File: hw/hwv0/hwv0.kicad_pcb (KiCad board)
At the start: 2 copper layers, 29 parts, among them J1 AVR-ISP-6, J2 PWR_IN_7-12V, J3 RS232, SW1 SW_Push, U1 ATtiny84A-MU, U2 LCD_1602, U3 MAX232I, U4 L7805

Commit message: Almost completed PCB
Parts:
- moved C5 91.4 mm to (103.1, 151.3), turned to 0 degrees
- moved SW1 91.2 mm to (83.6, 150.8), turned to 90 degrees
- moved TP7 89.5 mm to (108.7, 154.2)
- moved TP6 85.0 mm to (111.4, 154.3)
- moved J3 80.1 mm to (121.7, 139.3)
- moved U3 77.7 mm to (109.2, 146.1)
- moved C6 77.3 mm to (103.2, 149.7)
- moved C4 77.2 mm to (103.9, 146.1)
- moved C3 77.1 mm to (103.9, 142.9)
- moved C8 76.4 mm to (75.8, 154.5), turned to 0 degrees
- moved StrainGauge1 73.1 mm to (97.2, 158.4), turned to 180 degrees
- moved R1 70.2 mm to (92.1, 145.0), turned to 0 degrees
- moved D1 68.8 mm to (92.1, 142.9), turned to 180 degrees
- moved J1 67.7 mm to (94.8, 137.6), turned to 270 degrees
- moved TP2 66.6 mm to (83.2, 157.3), turned to 0 degrees
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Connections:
- J1 pad 1: (no net) -> /MISO
- J1 pad 3: (no net) -> /SCK
- J1 pad 4: (no net) -> /MOSI
- StrainGauge1 pad 3: /STRAINGAUGE- -> /SCK
- TP4 pad 1: /STRAINGAUGE- -> /SCK
- U1 pad 1: /STRAINGAUGE- -> /SCK
- U1 pad 16: Net-(U1-Pad16) -> /MOSI
- U1 pad 20: Net-(U1-Pad20) -> /MISO
- U2 pad 13: Net-(U1-Pad16) -> /MOSI
- U2 pad 14: Net-(U1-Pad20) -> /MISO
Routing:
- net +5V: track 0.00 -> 196.1 mm
- net GNDD: track 0.00 -> 146.3 mm
- net /MISO: track 0.00 -> 91.7 mm
- net /MOSI: track 0.00 -> 87.7 mm, vias 0 -> 1
- net Net-(U1-Pad15): track 0.00 -> 68.5 mm
- net /RX_L: track 0.00 -> 58.1 mm
- net /SCK: track 0.00 -> 49.8 mm
- net /~RST: track 0.00 -> 49.8 mm, vias 0 -> 1
- net /TX_L: track 0.00 -> 44.6 mm
- net /STRAINGAUGE+: track 0.00 -> 41.9 mm
- net /P_sen_analogIN: track 0.00 -> 23.9 mm
- net Net-(U1-Pad11): track 0.00 -> 19.1 mm
- net Net-(U1-Pad14): track 0.00 -> 18.0 mm
- net /RX_H: track 0.00 -> 16.6 mm
- net Net-(C5-Pad2): track 0.00 -> 15.5 mm
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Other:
- board outline added: 60.3 x 54.6 mm
- net class Default: trace_width 0.25 -> 0.3

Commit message: finished PCB
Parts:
- moved C8 2.02 mm to (77.8, 154.6)
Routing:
- net +5V: track 196.1 -> 250.8 mm
- net Net-(C7-Pad1): track 0.00 -> 20.8 mm
- added copper zone on B.Cu, net GNDD
- added copper zone on F.Cu, net GNDD
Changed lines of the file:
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@@
     (thickness 1.6)
     (drawings 6)
-    (tracks 260)
+    (tracks 281)
     (zones 0)
     (modules 29)
@@
   )
   (module Capacitor_SMD:CP_Elec_6.3x3 (layer F.Cu)
-    (at 75.7555 154.4955)
+    (at 77.7748 154.6352)
     (descr "SMT capacitor, aluminium electrolytic, 6.3x3, Nichicon ")
     (tags "Capacitor Electrolytic")
@@
   (segment (start 95.631 118.999) (end 95.631 120.269) (width 0.3) (layer F.Cu) (net 1))
   (segment (start 95.9485 118.6815) (end 95.631 118.999) (width 0.3) (layer F.Cu) (net 1))
+  (segment (start 97.1785 158.4325) (end 97.1785 160.0219) (width 0.5) (layer F.Cu) (net 1))
+  (segment (start 97.1785 160.0219) (end 96.3676 160.8328) (width 0.5) (layer F.Cu) (net 1))
+  (segment (start 96.3676 160.8328) (end 88.2904 160.8328) (width 0.5) (layer F.Cu) (net 1))
+  (segment (start 75.0748 150.9463) (end 73.05 148.9215) (width 1) (layer F.Cu) (net 1))
+  (segment (start 75.0748 154.6352) (end 75.0748 150.9463) (width 1) (layer F.Cu) (net 1))
+  (segment (start 88.2904 160.8328) (end 77.0636 160.8328) (width 0.5) (layer F.Cu) (net 1))
+  (segment (start 75.0748 158.844) (end 75.0748 154.6352) (width 0.5) (layer F.Cu) (net 1))
+  (segment (start 77.0636 160.8328) (end 75.0748 158.844) (width 0.5) (layer F.Cu) (net 1))
+  (segment (start 92.888 147.4976) (end 92.888 145.034) (width 0.5) (layer F.Cu) (net 1))
+  (segment (start 90.5764 149.8092) (end 92.888 147.4976) (width 0.5) (layer F.Cu) (net 1))
+  (segment (start 90.5764 153.3144) (end 90.5764 149.8092) (width 0.5) (layer F.Cu) (net 1))
+  (segment (start 87.3252 156.5656) (end 90.5764 153.3144) (width 0.5) (layer F.Cu) (net 1))
+  (segment (start 88.2904 160.8328) (end 87.3252 160.8328) (width 0.5) (layer F.Cu) (net 1))
+  (segment (start 87.3252 160.8328) (end 87.3252 156.5656) (width 0.5) (layer F.Cu) (net 1))
   (segment (start 76.2 116.300393) (end 76.10405 116.204443) (width 0.25) (layer F.Cu) (net 2))
   (segment (start 76.2 121.92) (end 76.2 116.300393) (width 0.25) (layer F.Cu) (net 2))
@@
   (segment (start 93.649451 150.064249) (end 93.649451 150.818555) (width 0.2) (layer F.Cu) (net 12))
   (segment (start 94.7082 149.0055) (end 93.649451 150.064249) (width 0.2) (layer F.Cu) (net 12))
-  (segment (start 92.1785 153.266605) (end 92.027451 153.115556) (width 0.3) (layer F.Cu) (net 24))
-  (segment (start 92.1785 158.4325) (end 92.1785 153.266605) (width 0.3) (layer F.Cu) (net 24))
-  (segment (start 92.027451 151.990555) (end 93.199451 150.818555) (width 0.2) (layer F.Cu) (net 24))
-  (segment (start 92.027451 153.115556) (end 92.027451 151.990555) (width 0.2) (layer F.Cu) (net 24))
-  (segment (start 98.675433 125.735663) (end 99.075433 125.735663) (width 0.2) (layer F.Cu) (net 24))
-  (segment (start 99.075433 125.735663) (end 99.100433 125.710663) (width 0.2) (layer F.Cu) (net 24))
-  (segment (start 99.100433 125.710663) (end 100.373463 125.710663) (width 0.2) (layer F.Cu) (net 24))
-  (segment (start 100.373463 125.710663) (end 101.9465 127.2837) (width 0.2) (layer F.Cu) (net 24))
-  (segment (start 101.9465 127.2837) (end 101.9465 138.5273) (width 0.2) (layer F.Cu) (net 24))
-  (segment (start 99.4065 141.0673) (end 99.4065 146.8458) (width 0.2) (layer F.Cu) (net 24))
-  (segment (start 99.4065 146.8458) (end 97.6968 148.5555) (width 0.2) (layer F.Cu) (net 24))
-  (segment (start 97.6968 148.5555) (end 94.5218 148.5555) (width 0.2) (layer F.Cu) (net 24))
-  (segment (start 94.5218 148.5555) (end 93.199451 149.877849) (width 0.2) (layer F.Cu) (net 24))
-  (segment (start 93.199451 149.877849) (end 93.199451 150.818555) (width 0.2) (layer F.Cu) (net 24))
   (segment (start 111.898557 146.73705) (end 114.16155 146.73705) (width 0.3) (layer F.Cu) (net 13))
   (segment (start 114.16155 146.73705) (end 115.443 148.0185) (width 0.3) (layer F.Cu) (net 13))
@@
   (segment (start 121.700556 144.855049) (end 116.407049 144.855049) (width 0.4) (layer F.Cu) (net 20))
   (segment (start 116.407049 144.855049) (end 115.74905 144.19705) (width 0.4) (layer F.Cu) (net 20))
+  (segment (start 76.6807 135.8665) (end 73.9775 135.8665) (width 1) (layer F.Cu) (net 21))
+  (segment (start 81.4705 134.3965) (end 78.1507 134.3965) (width 1) (layer F.Cu) (net 21))
+  (segment (start 78.1507 134.3965) (end 76.6807 135.8665) (width 1) (layer F.Cu) (net 21))
+  (segment (start 73.3 144.3215) (end 73.05 144.3215) (width 1) (layer F.Cu) (net 21))
+  (segment (start 76.6064 141.0151) (end 73.3 144.3215) (width 1) (layer F.Cu) (net 21))
+  (segment (start 76.6064 135.8392) (end 76.6064 141.0151) (width 1) (layer F.Cu) (net 21))
+  (segment (start 73.9775 135.8665) (end 76.5791 135.8665) (width 1) (layer F.Cu) (net 21))
+  (segment (start 76.5791 135.8665) (end 76.6064 135.8392) (width 1) (layer F.Cu) (net 21))
   (segment (start 114.20405 119.34895) (end 114.173 119.38) (width 0.4) (layer F.Cu) (net 22))
   (segment (start 114.173 116.235493) (end 114.20405 116.204443) (width 0.3) (layer F.Cu) (net 22))
@@
   (segment (start 94.757951 131.316855) (end 94.251096 130.81) (width 0.25) (layer F.Cu) (net 23))
   (segment (start 94.757951 137.558056) (end 94.757951 131.316855) (width 0.25) (layer F.Cu) (net 23))
+  (segment (start 92.1785 153.266605) (end 92.027451 153.115556) (width 0.3) (layer F.Cu) (net 24))
+  (segment (start 92.1785 158.4325) (end 92.1785 153.266605) (width 0.3) (layer F.Cu) (net 24))
+  (segment (start 92.027451 151.990555) (end 93.199451 150.818555) (width 0.2) (layer F.Cu) (net 24))
+  (segment (start 92.027451 153.115556) (end 92.027451 151.990555) (width 0.2) (layer F.Cu) (net 24))
+  (segment (start 98.675433 125.735663) (end 99.075433 125.735663) (width 0.2) (layer F.Cu) (net 24))
+  (segment (start 99.075433 125.735663) (end 99.100433 125.710663) (width 0.2) (layer F.Cu) (net 24))
+  (segment (start 99.100433 125.710663) (end 100.373463 125.710663) (width 0.2) (layer F.Cu) (net 24))
+  (segment (start 100.373463 125.710663) (end 101.9465 127.2837) (width 0.2) (layer F.Cu) (net 24))
+  (segment (start 101.9465 127.2837) (end 101.9465 138.5273) (width 0.2) (layer F.Cu) (net 24))
+  (segment (start 99.4065 141.0673) (end 99.4065 146.8458) (width 0.2) (layer F.Cu) (net 24))
+  (segment (start 99.4065 146.8458) (end 97.6968 148.5555) (width 0.2) (layer F.Cu) (net 24))
+  (segment (start 97.6968 148.5555) (end 94.5218 148.5555) (width 0.2) (layer F.Cu) (net 24))
+  (segment (start 94.5218 148.5555) (end 93.199451 149.877849) (width 0.2) (layer F.Cu) (net 24))
+  (segment (start 93.199451 149.877849) (end 93.199451 150.818555) (width 0.2) (layer F.Cu) (net 24))
   (segment (start 101.9465 138.5273) (end 99.441 141.0328) (width 0.2) (layer F.Cu) (net 24))
   (segment (start 99.441 141.0328) (end 99.4065 141.0673) (width 0.2) (layer F.Cu) (net 24))
-  (segment (start 99.441 140.97) (end 99.441 141.0328) (width 0.3) (layer F.Cu) (net 24))
-  (segment (start 97.282 138.811) (end 99.441 140.97) (width 0.3) (layer F.Cu) (net 24))
-  (segment (start 92.217951 137.558056) (end 93.470895 138.811) (width 0.3) (layer F.Cu) (net 24))
-  (segment (start 93.470895 138.811) (end 97.282 138.811) (width 0.3) (layer F.Cu) (net 24))
+  (segment (start 97.3582 138.8872) (end 99.441 140.97) (width 0.3) (layer F.Cu) (net 24))
+  (segment (start 92.217951 137.558056) (end 93.547095 138.8872) (width 0.3) (layer F.Cu) (net 24))
+  (segment (start 93.547095 138.8872) (end 97.3582 138.8872) (width 0.3) (layer F.Cu) (net 24))
   (segment (start 75.82041 129.667) (end 92.344096 129.667) (width 0.25) (layer F.Cu) (net 25))
   (segment (start 106.58405 116.204443) (end 101.827618 111.448011) (width 0.25) (layer F.Cu) (net 25))
@@
   (segment (start 92.217951 140.098056) (end 90.9955 138.875605) (width 0.3) (layer B.Cu) (net 25))
   (segment (start 90.9955 138.875605) (end 90.9955 131.015596) (width 0.3) (layer B.Cu) (net 25))
+  (zone (net 2) (net_name GNDD) (layer B.Cu) (hatch none 0.508)
+    (connect_pads (clearance 0.508))
+    (min_thickness 0.254)
+    (fill yes (arc_segments 16) (thermal_gap 0.508) (thermal_bridge_width 0.508))
+    (polygon
+      (pts
+        (xy 69.85 109.855) (xy 130.175 109.855) (xy 130.175 164.465) (xy 69.85 164.465)
+      )
+    )
+  )
+  (zone (net 2) (net_name GNDD) (layer F.Cu) (hatch none 0.508)
+    (connect_pads (clearance 0.508))
+    (min_thickness 0.254)
+    (fill yes (arc_segments 16) (thermal_gap 0.508) (thermal_bridge_width 0.508))
+    (polygon
+      (pts
+        (xy 69.85 109.855) (xy 130.175 109.855) (xy 130.175 164.465) (xy 69.85 164.465)
+      )
+    )
+  )
 )

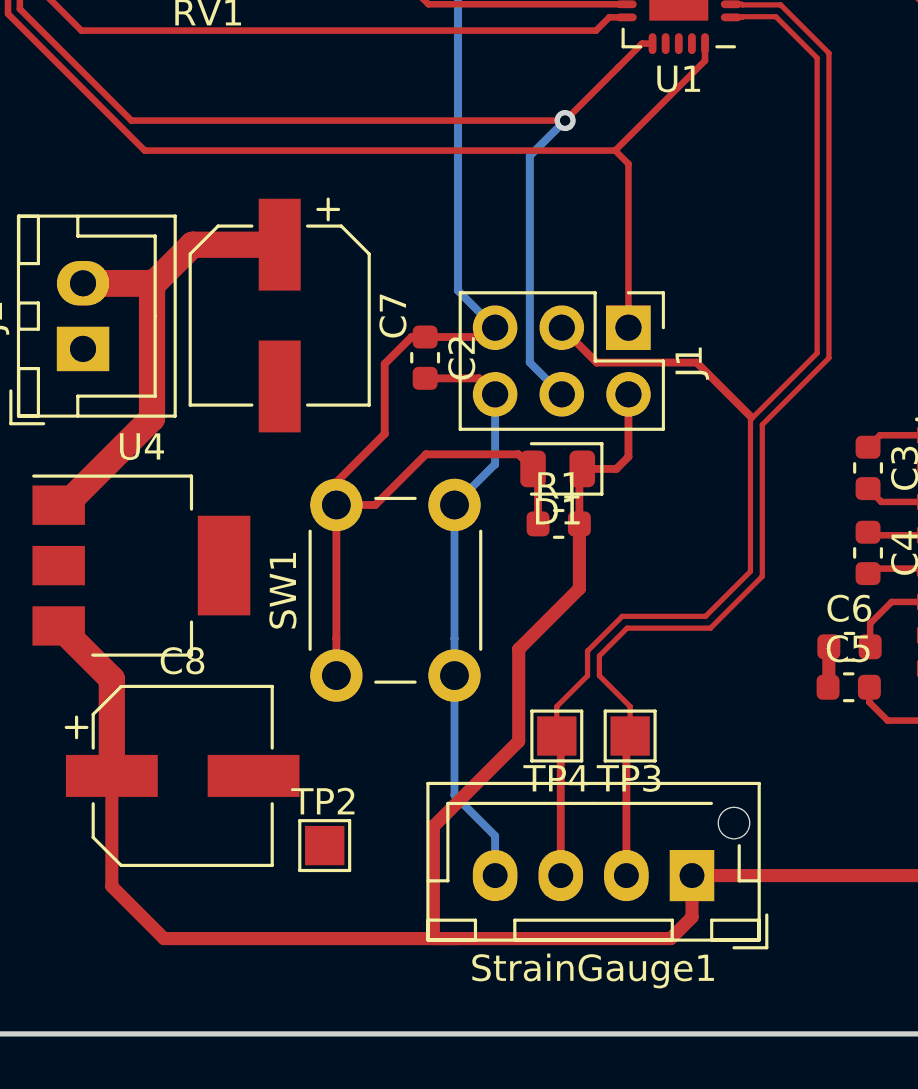
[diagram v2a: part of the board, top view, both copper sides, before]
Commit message: made schematic more clear
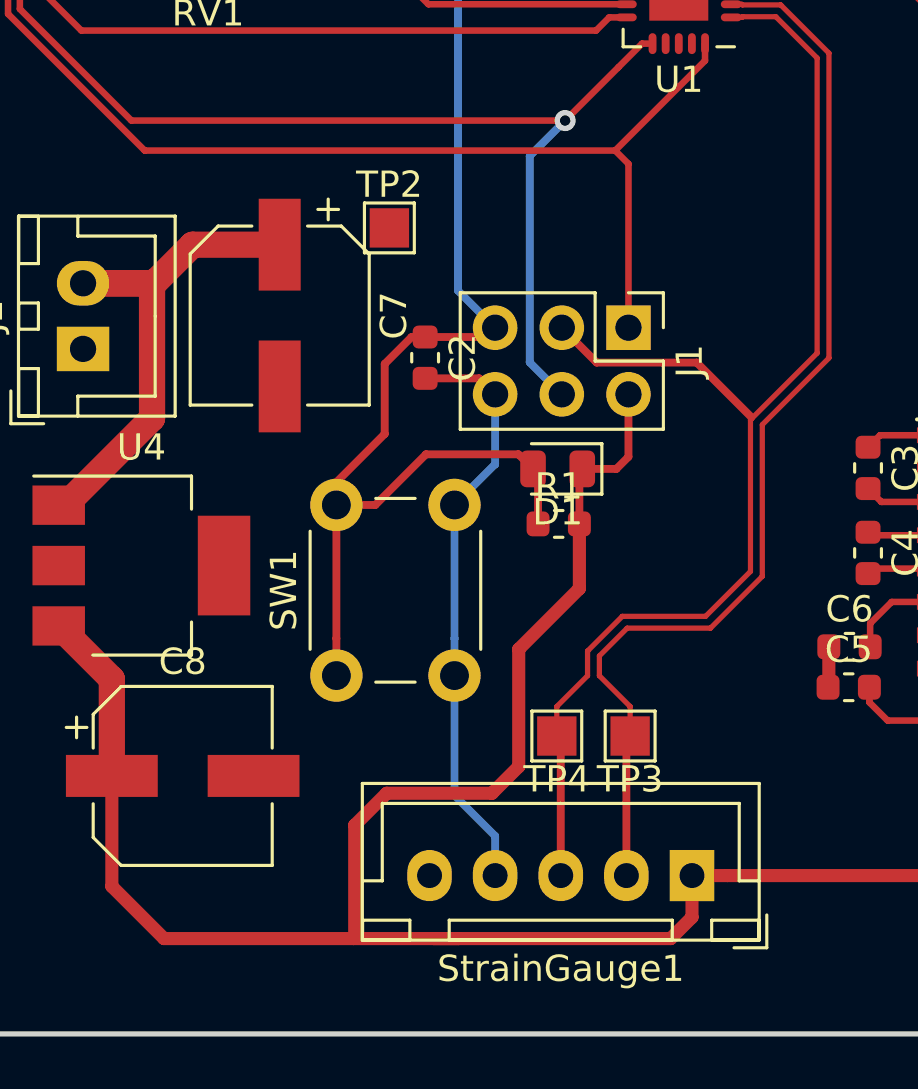
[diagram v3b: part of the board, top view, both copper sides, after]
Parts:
- StrainGauge1: value Conn_01x04_Female -> Conn_01x04_Shielded; footprint Connector_JST:JST_XH_B04B-XH-AM_1x04_P2.50mm_Vertical -> Connector_JST:JST_XH_B05B-XH-A_1x05_P2.50mm_Vertical
- moved TP2 23.7 mm to (85.6, 133.8)
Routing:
- net +5V: track 250.8 -> 254.4 mm

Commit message: stitched PCB
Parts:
- moved TP1 1.52 mm to (103.3, 119.2)
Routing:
- net GNDD: track 146.3 -> 135.1 mm, vias 0 -> 64
- net Net-(U1-Pad15): track 68.5 -> 62.3 mm
- net /MISO: track 91.7 -> 86.7 mm
- net /MOSI: track 87.7 -> 83.1 mm
- net +5V: track 254.4 -> 251.2 mm
- net Net-(U1-Pad11): track 19.1 -> 16.9 mm
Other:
- outline, holes or cut-outs redrawn
